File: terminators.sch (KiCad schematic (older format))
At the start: 13 parts, among them U37 74LS32

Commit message: Begin adding part numbers
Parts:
- U37: Optional (none) -> PARALLEL/FLOPPY/KEYBOARD
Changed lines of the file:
@@
 F 2 "Package_DIP:DIP-14_W7.62mm_Socket_LongPads" H 8660 5205 50  0001 C CNN
 F 3 "http://www.ti.com/lit/gpn/sn74LS32" H 8660 5205 50  0001 C CNN
+F 4 "PARALLEL/FLOPPY/KEYBOARD" H 8660 5205 50  0001 C CNN "Optional"
 	4    8660 5205
 	1    0    0    -1
@@
 F 2 "Package_DIP:DIP-14_W7.62mm_Socket_LongPads" H 9625 5680 50  0001 C CNN
 F 3 "http://www.ti.com/lit/gpn/sn74LS32" H 9625 5680 50  0001 C CNN
+F 4 "PARALLEL/FLOPPY/KEYBOARD" H 9625 5680 50  0001 C CNN "Optional"
 	3    9625 5680
 	1    0    0    -1

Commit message: More part numbers
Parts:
- U37: Cost (none) -> 0.442; MFG Name (none) -> TI; MFG Part Num (none) -> SN74LS32N
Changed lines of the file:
@@
 F 3 "http://www.ti.com/lit/gpn/sn74LS32" H 8660 5205 50  0001 C CNN
 F 4 "PARALLEL/FLOPPY/KEYBOARD" H 8660 5205 50  0001 C CNN "Optional"
+F 5 "0.442" H 8660 5205 50  0001 C CNN "Cost"
+F 6 "TI" H 8660 5205 50  0001 C CNN "MFG Name"
+F 7 "SN74LS32N" H 8660 5205 50  0001 C CNN "MFG Part Num"
 	4    8660 5205
 	1    0    0    -1
@@
 F 3 "http://www.ti.com/lit/gpn/sn74LS32" H 9625 5680 50  0001 C CNN
 F 4 "PARALLEL/FLOPPY/KEYBOARD" H 9625 5680 50  0001 C CNN "Optional"
+F 5 "0.442" H 9625 5680 50  0001 C CNN "Cost"
+F 6 "TI" H 9625 5680 50  0001 C CNN "MFG Name"
+F 7 "SN74LS32N" H 9625 5680 50  0001 C CNN "MFG Part Num"
 	3    9625 5680
 	1    0    0    -1

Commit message: (Try to) Identify the minimum set of required components
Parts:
- U37: Required (none) -> Y
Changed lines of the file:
@@
 F 6 "TI" H 8660 5205 50  0001 C CNN "MFG Name"
 F 7 "SN74LS32N" H 8660 5205 50  0001 C CNN "MFG Part Num"
+F 8 "Y" H 8660 5205 50  0001 C CNN "Required"
 	4    8660 5205
 	1    0    0    -1
@@
 F 6 "TI" H 9625 5680 50  0001 C CNN "MFG Name"
 F 7 "SN74LS32N" H 9625 5680 50  0001 C CNN "MFG Part Num"
+F 8 "Y" H 9625 5680 50  0001 C CNN "Required"
 	3    9625 5680
 	1    0    0    -1

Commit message: Rename "Optional" Field to "Section"
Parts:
- U37: Optional PARALLEL/FLOPPY/KEYBOARD -> (none); Section (none) -> PARALLEL/FLOPPY/KEYBOARD
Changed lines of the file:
@@
 F 2 "Package_DIP:DIP-14_W7.62mm_Socket_LongPads" H 8660 5205 50  0001 C CNN
 F 3 "http://www.ti.com/lit/gpn/sn74LS32" H 8660 5205 50  0001 C CNN
-F 4 "PARALLEL/FLOPPY/KEYBOARD" H 8660 5205 50  0001 C CNN "Optional"
+F 4 "PARALLEL/FLOPPY/KEYBOARD" H 8660 5205 50  0001 C CNN "Section"
 F 5 "0.442" H 8660 5205 50  0001 C CNN "Cost"
 F 6 "TI" H 8660 5205 50  0001 C CNN "MFG Name"
@@
 F 2 "Package_DIP:DIP-14_W7.62mm_Socket_LongPads" H 9625 5680 50  0001 C CNN
 F 3 "http://www.ti.com/lit/gpn/sn74LS32" H 9625 5680 50  0001 C CNN
-F 4 "PARALLEL/FLOPPY/KEYBOARD" H 9625 5680 50  0001 C CNN "Optional"
+F 4 "PARALLEL/FLOPPY/KEYBOARD" H 9625 5680 50  0001 C CNN "Section"
 F 5 "0.442" H 9625 5680 50  0001 C CNN "Cost"
 F 6 "TI" H 9625 5680 50  0001 C CNN "MFG Name"

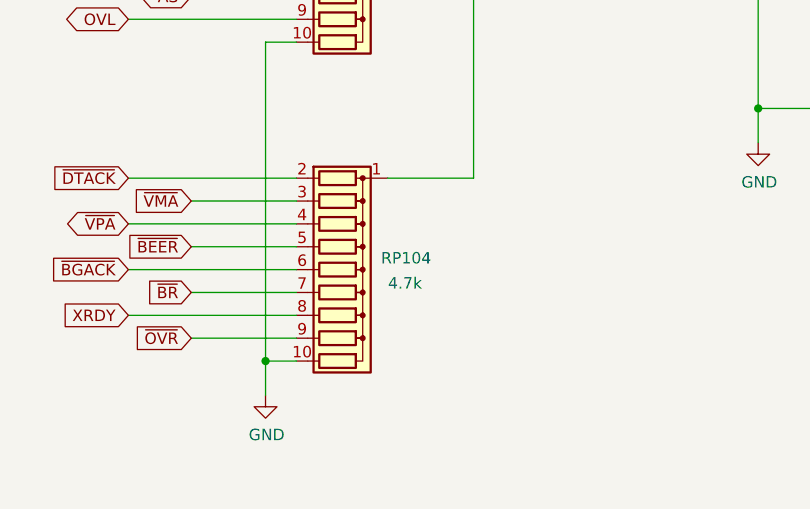
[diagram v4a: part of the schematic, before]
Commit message: RP104 -> 470R
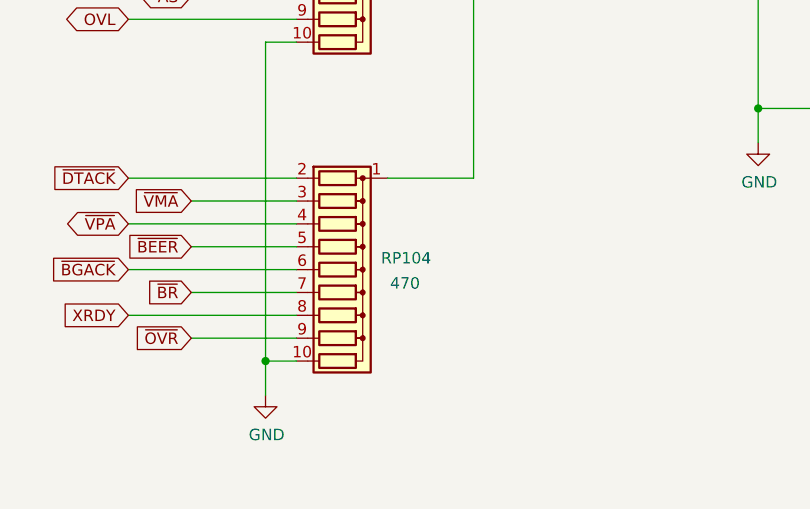
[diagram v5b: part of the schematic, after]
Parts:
- RP104: value 4.7k -> 470
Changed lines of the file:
@@
 Sheet 8 14
 Title "Rämixx500"
-Date "2019-04-20"
+Date "2021-05-16"
 Rev "1"
 Comp "SukkoPera"
@@
 P 6300 6485
 F 0 "RP104" V 6250 6765 50  0000 C CNN
-F 1 "4.7k" V 6360 6760 50  0000 C CNN
+F 1 "470" V 6360 6760 50  0000 C CNN
 F 2 "Resistor_THT:R_Array_SIP10" V 6875 6485 50  0001 C CNN
 F 3 "http://www.vishay.com/docs/31509/csc.pdf" H 6300 6485 50  0001 C CNN
